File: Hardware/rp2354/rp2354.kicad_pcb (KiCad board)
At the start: 4 copper layers, 20 x 29 mm, 30 parts, among them U1 RP2354A, Y1 ABM8-272-T3

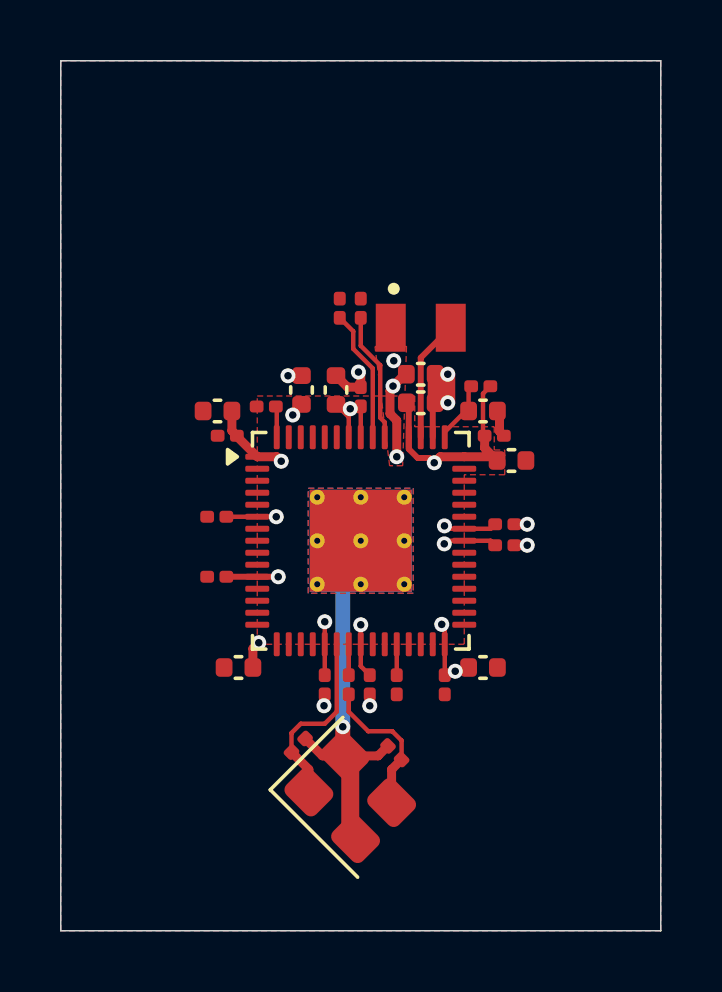
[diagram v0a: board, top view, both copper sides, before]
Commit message: Avoid using zones in the RP2354A design block
Using zones in design blocks doesn't seem to work very well in practice,
at least in the version I have (10.0.4).

I'm not entirely sure what is going on, but what seems to happen is that
when a design block is imported into a PCB design (with the "update pcb
from schematic" workflow), kicad will import it as a group, but then try
to merge matching zones with the outside.  And really confuse the
grouping as a result, and also end up mixing up the zones occasionally
so that the zone names are just completely wrong and misleading.

Sometimes it gets so bad that you end up with zones that you can see on
the PCB, but not actually access from the UI.  No way to delete the
stale zombie left-overs.  At one point I ended up rescuing one PCB by
editing the kicad_pcb file by hand and removing a group that seemed to
only exist as a grouping of zombie zones that no longer existed in
reality.

NOTE! The above is purely a symptom description from what I've seen, not
any kind of deeper understanding of what kicad actually does.  There
might be something entirely else going on, and I'm just confused.

Whatever the real issue is, zones _work_, but they seem to have a
propensity for causing problems, and I've never seen it with normal
elements.  The TAC5242 design never caused me any problems - it doesn't
use any zones (except for the base ground plane that isn't part of the
design block export).

Anyway, I can just route the power rails under the RP2354 manually using
actual traces.  It's not like it's even all that complicated: the zones
were there just to tie the room together.

Let's see if this gets rid of some of the oddities of using pre-routed
design blocks.

Signed-off-by: Linus Torvalds <torvalds@linux-foundation.org>
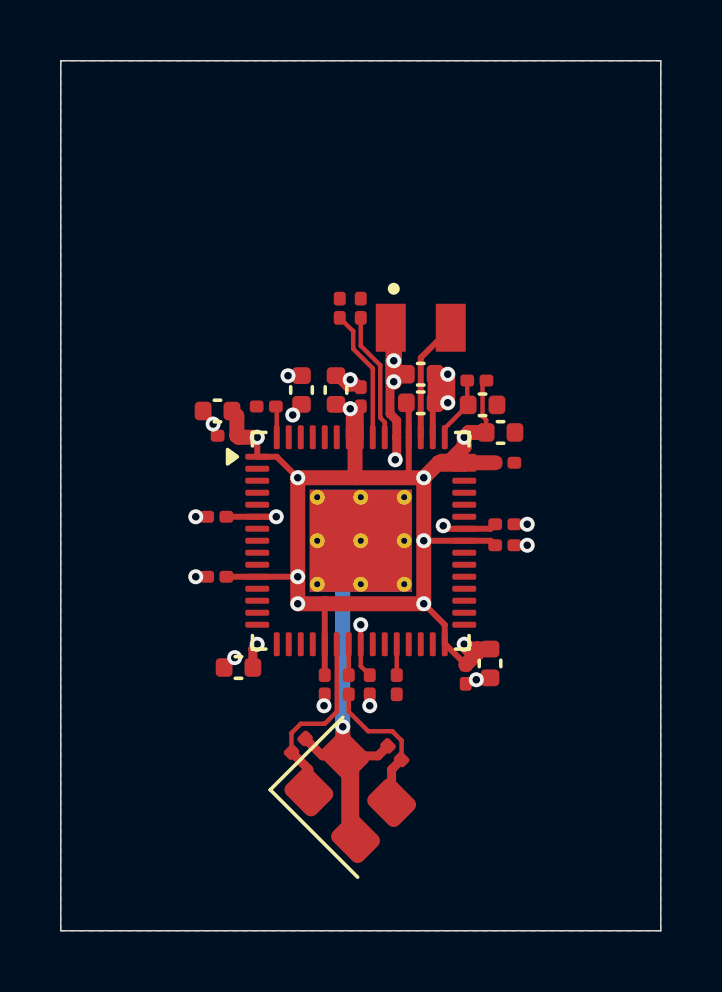
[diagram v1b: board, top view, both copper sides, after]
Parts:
- moved C21 1.00 mm to (104.7, 96.4)
- moved C14 0.97 mm to (104.8, 97.4)
- moved C13 0.78 mm to (103.5, 104.5)
- moved C19 0.27 mm to (104.3, 104.1), turned to -90 degrees
- moved R1 0.23 mm to (103.9, 94.7)
- moved C5 0.21 mm to (104.1, 95.5)
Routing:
- net +3V3: track 24.8 -> 71.4 mm, vias 9 -> 11
- net +1V1: track 12.6 -> 30.4 mm
- net GND: track 19.0 -> 18.0 mm, vias 9 -> 14
- removed copper zone on F.Cu, net +1V1
- removed copper zone on In2.Cu, net +1V1
- removed copper zone on F.Cu, net +3V3
- removed copper zone on In1.Cu, net +3V3
